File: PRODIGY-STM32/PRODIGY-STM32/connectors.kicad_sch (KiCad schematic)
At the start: 1 part, among them J1 DF40C-100DS-0.4V(51)

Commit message: stm32 schematic finished
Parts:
- added FID4, FID5: Fiducial, symbol Mechanical:Fiducial
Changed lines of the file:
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@@
 		(dnp no)
 		(fields_autoplaced yes)
-		(property "Reference" "#PWR018"
+		(property "Reference" "#PWR021"
 			(at 146.05 170.18 0)
 			(effects
@@
 			(project "PRODIGY-STM32"
 				(path "/f2f1c781-b8fe-416b-b7a0-b424640c1d9f/333eab81-c884-4b42-882a-4ee6d949c24e"
-					(reference "#PWR018")
+					(reference "#PWR021")
 					(unit 1)
 				)
@@
 	)
 	(symbol
+		(lib_id "Mechanical:Fiducial")
+		(at 186.69 33.02 0)
+		(unit 1)
+		(exclude_from_sim no)
+		(in_bom yes)
+		(on_board yes)
+		(dnp no)
+		(fields_autoplaced yes)
+		(property "Reference" "FID4"
+			(at 189.23 31.7499 0)
+			(effects
+				(font
+					(size 1.27 1.27)
+				)
+				(justify left)
+			)
+		)
+		(property "Value" "Fiducial"
+			(at 189.23 34.2899 0)
+			(effects
+				(font
+					(size 1.27 1.27)
+				)
+				(justify left)
+			)
+		)
+		(property "Footprint" ""
+			(at 186.69 33.02 0)
+			(effects
+				(font
+					(size 1.27 1.27)
+				)
+				(hide yes)
+			)
+		)
+		(property "Datasheet" "~"
+			(at 186.69 33.02 0)
+			(effects
+				(font
+					(size 1.27 1.27)
+				)
+				(hide yes)
+			)
+		)
+		(property "Description" "Fiducial Marker"
+			(at 186.69 33.02 0)
+			(effects
+				(font
+					(size 1.27 1.27)
+				)
+				(hide yes)
+			)
+		)
+		(instances
+			(project "PRODIGY-STM32"
+				(path "/f2f1c781-b8fe-416b-b7a0-b424640c1d9f/333eab81-c884-4b42-882a-4ee6d949c24e"
+					(reference "FID4")
+					(unit 1)
+				)
+			)
+		)
+	)
+	(symbol
 		(lib_id "power:GND")
 		(at 128.27 163.83 0)
@@
 		(dnp no)
 		(fields_autoplaced yes)
-		(property "Reference" "#PWR017"
+		(property "Reference" "#PWR020"
 			(at 128.27 170.18 0)
 			(effects
@@
 			(project "PRODIGY-STM32"
 				(path "/f2f1c781-b8fe-416b-b7a0-b424640c1d9f/333eab81-c884-4b42-882a-4ee6d949c24e"
-					(reference "#PWR017")
+					(reference "#PWR020")
 					(unit 1)
 				)
+			)
+		)
+	)
+	(symbol
+		(lib_id "Mechanical:Fiducial")
+		(at 186.69 39.37 0)
+		(unit 1)
+		(exclude_from_sim no)
+		(in_bom yes)
+		(on_board yes)
+		(dnp no)
+		(fields_autoplaced yes)
+		(property "Reference" "FID5"
+			(at 189.23 38.0999 0)
+			(effects
+				(font
+					(size 1.27 1.27)
+				)
+				(justify left)
+			)
+		)
+		(property "Value" "Fiducial"
+			(at 189.23 40.6399 0)
+			(effects
+				(font
+					(size 1.27 1.27)
+				)
+				(justify left)
+			)
+		)
+		(property "Footprint" ""
+			(at 186.69 39.37 0)
+			(effects
+				(font
+					(size 1.27 1.27)
+				)
+				(hide yes)
+			)
+		)
+		(property "Datasheet" "~"
+			(at 186.69 39.37 0)
+			(effects
+				(font
+					(size 1.27 1.27)
+				)
+				(hide yes)
+			)
+		)
+		(property "Description" "Fiducial Marker"
+			(at 186.69 39.37 0)
+			(effects
+				(font
+					(size 1.27 1.27)
+				)
+				(hide yes)
+			)
+		)
+		(instances
+			(project "PRODIGY-STM32"
+				(path "/f2f1c781-b8fe-416b-b7a0-b424640c1d9f/333eab81-c884-4b42-882a-4ee6d949c24e"
+					(reference "FID5")
+					(unit 1)
+				)

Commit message: All footprint assosiations have been made across all schematics.
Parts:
- removed FID4, FID5: Fiducial, symbol Mechanical:Fiducial
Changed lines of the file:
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@@
-	)
-	(symbol
-		(lib_id "Mechanical:Fiducial")
-		(at 186.69 33.02 0)
-		(unit 1)
-		(exclude_from_sim no)
-		(in_bom yes)
-		(on_board yes)
-		(dnp no)
-		(fields_autoplaced yes)
-		(property "Reference" "FID4"
-			(at 189.23 31.7499 0)
-			(effects
-				(font
-					(size 1.27 1.27)
-				)
-				(justify left)
-			)
-		)
-		(property "Value" "Fiducial"
-			(at 189.23 34.2899 0)
-			(effects
-				(font
-					(size 1.27 1.27)
-				)
-				(justify left)
-			)
-		)
-		(property "Footprint" ""
-			(at 186.69 33.02 0)
-			(effects
-				(font
-					(size 1.27 1.27)
-				)
-				(hide yes)
-			)
-		)
-		(property "Datasheet" "~"
-			(at 186.69 33.02 0)
-			(effects
-				(font
-					(size 1.27 1.27)
-				)
-				(hide yes)
-			)
-		)
-		(property "Description" "Fiducial Marker"
-			(at 186.69 33.02 0)
-			(effects
-				(font
-					(size 1.27 1.27)
-				)
-				(hide yes)
-			)
-		)
-		(instances
-			(project "PRODIGY-STM32"
-				(path "/f2f1c781-b8fe-416b-b7a0-b424640c1d9f/333eab81-c884-4b42-882a-4ee6d949c24e"
-					(reference "FID4")
-					(unit 1)
-				)
-			)
-		)
 	)
 	(symbol
@@
 					(unit 1)
 				)
-			)
-		)
-	)
-	(symbol
-		(lib_id "Mechanical:Fiducial")
-		(at 186.69 39.37 0)
-		(unit 1)
-		(exclude_from_sim no)
-		(in_bom yes)
-		(on_board yes)
-		(dnp no)
-		(fields_autoplaced yes)
-		(property "Reference" "FID5"
-			(at 189.23 38.0999 0)
-			(effects
-				(font
-					(size 1.27 1.27)
-				)
-				(justify left)
-			)
-		)
-		(property "Value" "Fiducial"
-			(at 189.23 40.6399 0)
-			(effects
-				(font
-					(size 1.27 1.27)
-				)
-				(justify left)
-			)
-		)
-		(property "Footprint" ""
-			(at 186.69 39.37 0)
-			(effects
-				(font
-					(size 1.27 1.27)
-				)
-				(hide yes)
-			)
-		)
-		(property "Datasheet" "~"
-			(at 186.69 39.37 0)
-			(effects
-				(font
-					(size 1.27 1.27)
-				)
-				(hide yes)
-			)
-		)
-		(property "Description" "Fiducial Marker"
-			(at 186.69 39.37 0)
-			(effects
-				(font
-					(size 1.27 1.27)
-				)
-				(hide yes)
-			)
-		)
-		(instances
-			(project "PRODIGY-STM32"
-				(path "/f2f1c781-b8fe-416b-b7a0-b424640c1d9f/333eab81-c884-4b42-882a-4ee6d949c24e"
-					(reference "FID5")
-					(unit 1)
-				)

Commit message: STM32 bom done.
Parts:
- J1: value DF40C-100DS-0.4V(51) -> DF40C-100DP-04V-51; TME (none) -> DF40C-100DP-04V-51
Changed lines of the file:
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@@
 			)
 		)
-		(property "Value" "DF40C-100DS-0.4V(51)"
+		(property "Value" "DF40C-100DP-04V-51"
 			(at 137.16 28.194 0)
 			(effects
@@
 			(effects
 				(font
+					(size 1.27 1.27)
+				)
+				(hide yes)
+			)
+		)
+		(property "MOUSER" ""
+			(at 137.16 27.94 0)
+			(effects
+				(font
+					(size 1.27 1.27)
+				)
+				(hide yes)
+			)
+		)
+		(property "TME" "DF40C-100DP-04V-51"
+			(at 137.16 27.94 0)
+			(effects
+				(font

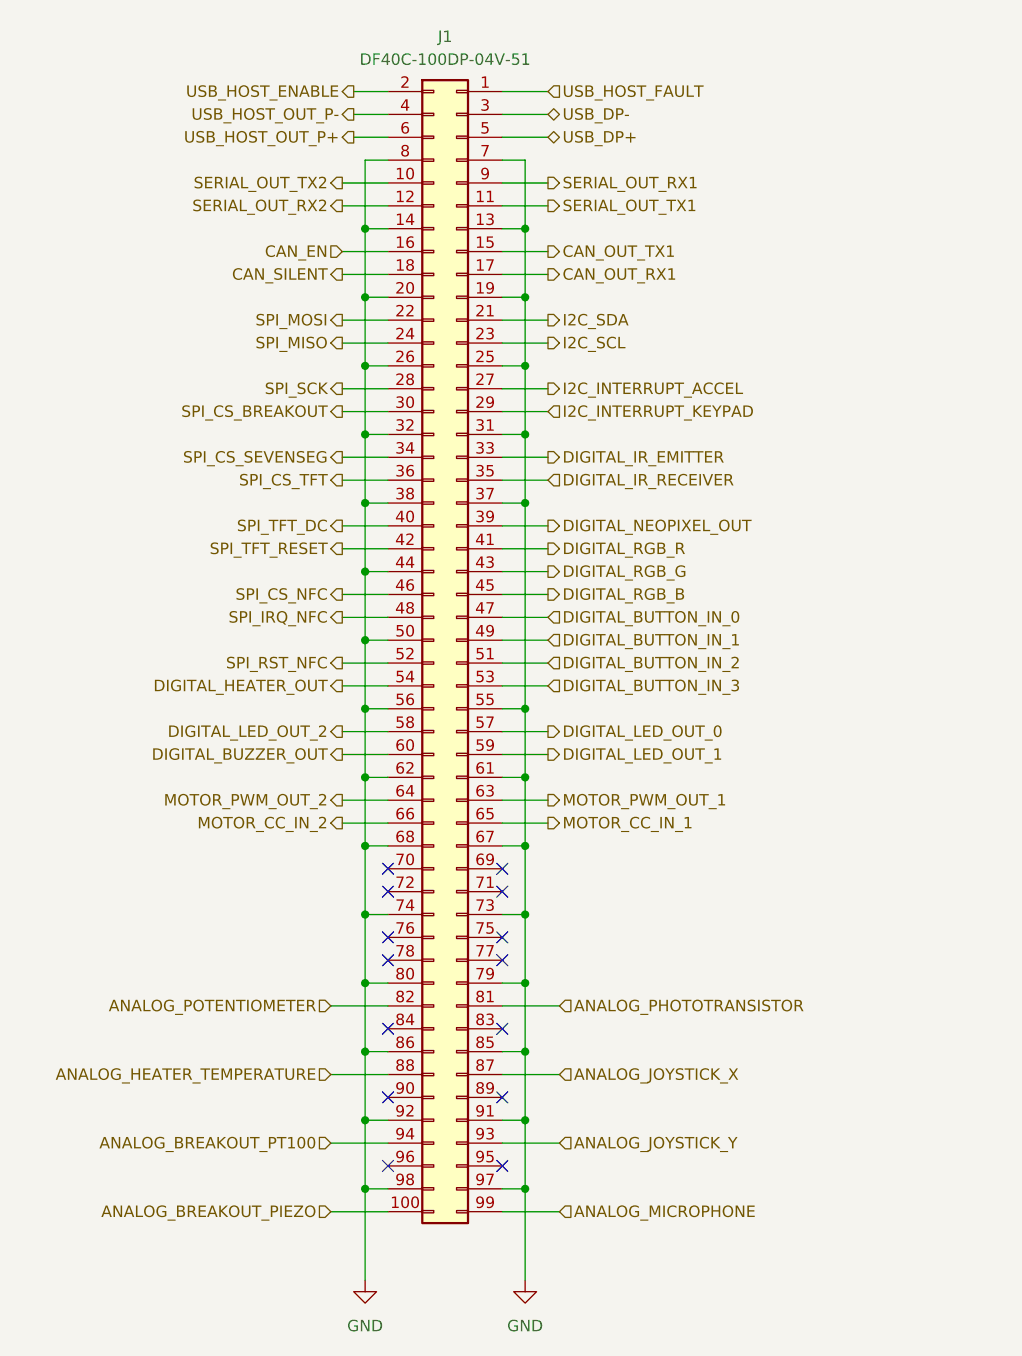
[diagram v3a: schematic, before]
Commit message: stm32 started, footprints updated, lazout started
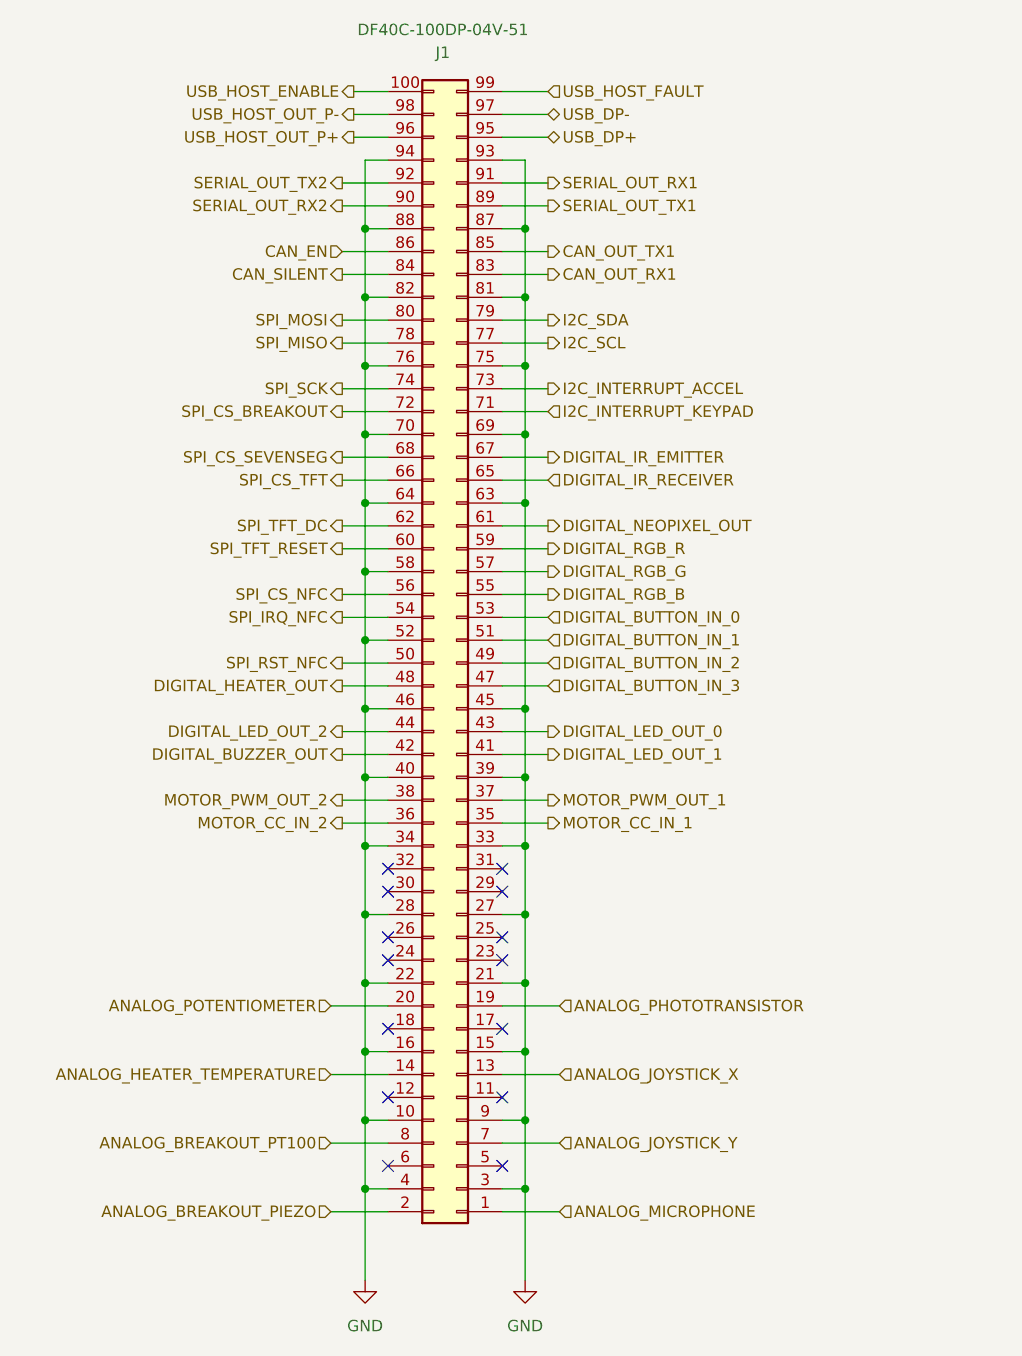
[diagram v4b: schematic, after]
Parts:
- J1: footprint DF40C:HIROSE_DF40C-100DS-0.4V_51_ -> DF40C-100DP-0:DF40C100DP04V51
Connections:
- net ANALOG_BREAKOUT_PIEZO: now also J1.2; no longer J1.100
- net ANALOG_BREAKOUT_PT100: now also J1.8; no longer J1.94
- net ANALOG_HEATER_TEMPERATURE: now also J1.14; no longer J1.88
- net ANALOG_JOYSTICK_X: now also J1.13; no longer J1.87
- net ANALOG_JOYSTICK_Y: now also J1.7; no longer J1.93
- net ANALOG_MICROPHONE: now also J1.1; no longer J1.99
- net ANALOG_PHOTOTRANSISTOR: now also J1.19; no longer J1.81
- net ANALOG_POTENTIOMETER: now also J1.20; no longer J1.82
- net CAN_EN: now also J1.86; no longer J1.16
- net CAN_OUT_RX1: now also J1.83; no longer J1.17
- net CAN_OUT_TX1: now also J1.85; no longer J1.15
- net CAN_SILENT: now also J1.84; no longer J1.18
- net DIGITAL_BUTTON_IN_0: now also J1.53; no longer J1.47
- net DIGITAL_BUTTON_IN_1: now also J1.51; no longer J1.49
- net DIGITAL_BUTTON_IN_2: now also J1.49; no longer J1.51
- net DIGITAL_BUTTON_IN_3: now also J1.47; no longer J1.53
- net DIGITAL_BUZZER_OUT: now also J1.42; no longer J1.60
- net DIGITAL_HEATER_OUT: now also J1.48; no longer J1.54
- net DIGITAL_IR_EMITTER: now also J1.67; no longer J1.33
- net DIGITAL_IR_RECEIVER: now also J1.65; no longer J1.35
- net DIGITAL_LED_OUT_0: now also J1.43; no longer J1.57
- net DIGITAL_LED_OUT_1: now also J1.41; no longer J1.59
- net DIGITAL_LED_OUT_2: now also J1.44; no longer J1.58
- net DIGITAL_NEOPIXEL_OUT: now also J1.61; no longer J1.39
- net DIGITAL_RGB_B: now also J1.55; no longer J1.45
- net DIGITAL_RGB_G: now also J1.57; no longer J1.43
- net DIGITAL_RGB_R: now also J1.59; no longer J1.41
- net GND: now also J1.10, J1.15, J1.16, J1.21, J1.22, J1.27, J1.28, J1.3, J1.33, J1.34, J1.39, J1.4, J1.40, J1.45, J1.46, J1.52, J1.58, J1.63, J1.64, J1.69, J1.70, J1.75, J1.76, J1.81, J1.82, J1.87, J1.88, J1.9, J1.93, J1.94; no longer J1.13, J1.14, J1.19, J1.20, J1.25, J1.26, J1.31, J1.32, J1.37, J1.38, J1.44, J1.50, J1.55, J1.56, J1.61, J1.62, J1.67, J1.68, J1.7, J1.73, J1.74, J1.79, J1.8, J1.80, J1.85, J1.86, J1.91, J1.92, J1.97, J1.98
- net I2C_INTERRUPT_ACCEL: now also J1.73; no longer J1.27
- net I2C_INTERRUPT_KEYPAD: now also J1.71; no longer J1.29
- net I2C_SCL: now also J1.77; no longer J1.23
- net I2C_SDA: now also J1.79; no longer J1.21
- net MOTOR_CC_IN_1: now also J1.35; no longer J1.65
- net MOTOR_CC_IN_2: now also J1.36; no longer J1.66
- net MOTOR_PWM_OUT_1: now also J1.37; no longer J1.63
- net MOTOR_PWM_OUT_2: now also J1.38; no longer J1.64
- net SERIAL_OUT_RX1: now also J1.91; no longer J1.9
- net SERIAL_OUT_RX2: now also J1.90; no longer J1.12
- net SERIAL_OUT_TX1: now also J1.89; no longer J1.11
- net SERIAL_OUT_TX2: now also J1.92; no longer J1.10
- net SPI_CS_BREAKOUT: now also J1.72; no longer J1.30
- net SPI_CS_NFC: now also J1.56; no longer J1.46
- net SPI_CS_SEVENSEG: now also J1.68; no longer J1.34
- net SPI_CS_TFT: now also J1.66; no longer J1.36
- net SPI_IRQ_NFC: now also J1.54; no longer J1.48
- net SPI_MISO: now also J1.78; no longer J1.24
- net SPI_MOSI: now also J1.80; no longer J1.22
- net SPI_RST_NFC: now also J1.50; no longer J1.52
- net SPI_SCK: now also J1.74; no longer J1.28
- net SPI_TFT_DC: now also J1.62; no longer J1.40
- net SPI_TFT_RESET: now also J1.60; no longer J1.42
- net USB_DP+: now also J1.95; no longer J1.5
- net USB_DP-: now also J1.97; no longer J1.3
- net USB_HOST_ENABLE: now also J1.100; no longer J1.2
- net USB_HOST_FAULT: now also J1.99; no longer J1.1
- net USB_HOST_OUT_P+: now also J1.96; no longer J1.6
- net USB_HOST_OUT_P-: now also J1.98; no longer J1.4
